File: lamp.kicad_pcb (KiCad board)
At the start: 2 copper layers, 83.8 x 40.6 mm, 18 parts, among them J1 Screw_Terminal_01x02, J2 Screw_Terminal_01x02, Q1 2N7002, U1 ESP-12E, U2 34.81-7048, U3 AMS1117-3.3

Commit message: some chnges
some changes
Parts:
- moved F1 27.5 mm to (130.2, 100.3), turned to -90 degrees
- moved U3 27.3 mm to (153.7, 124.5), turned to 180 degrees
- moved J1 24.1 mm to (121.9, 123.0)
- moved J2 20.6 mm to (121.9, 100.1)
- moved C3 12.2 mm to (167.6, 105.4), turned to -90 degrees
- moved Q1 8.54 mm to (156.2, 110.5)
- moved R6 7.86 mm to (152.4, 115.6)
- moved C4 6.87 mm to (163.8, 105.4), turned to -90 degrees
- moved C1 6.75 mm to (156.2, 118.1), turned to 0 degrees
- moved R2 6.68 mm to (176.5, 106.7)
- moved RV1 6.52 mm to (126.7, 116.8), turned to 90 degrees
- moved R3 5.56 mm to (181.6, 106.7)
- moved U2 5.43 mm to (156.5, 104.3)
- moved PS1 5.42 mm to (131.5, 121.9)
- moved R5 5.01 mm to (174.0, 129.5), turned to 90 degrees
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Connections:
- F1 pad 1: Net-(J2-Pad2) -> Net-(F1-Pad1)
- J1 pad 2: Net-(J2-Pad1) -> Net-(U2-Pad11)
- J2 pad 1: Net-(J2-Pad1) -> Net-(F1-Pad1)
- J2 pad 2: Net-(J2-Pad2) -> Net-(J1-Pad1)
- PS1 pad 2: Net-(J2-Pad1) -> Net-(J1-Pad1)
- RV1 pad 1: Net-(J2-Pad1) -> Net-(J1-Pad1)
- U2 pad 11: Net-(J1-Pad1) -> Net-(U2-Pad11)
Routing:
- net Net-(U2-Pad11): track 0.00 -> 46.1 mm
- net Net-(J2-Pad1): track 28.5 -> 0.00 mm
- net Net-(C1-Pad2): track 42.6 -> 15.1 mm
- net Net-(J1-Pad1): track 20.1 -> 33.8 mm
- net Net-(J2-Pad2): track 12.2 -> 0.00 mm
- net Net-(F1-Pad1): track 0.00 -> 8.38 mm
- net Net-(Q1-Pad1): track 44.9 -> 37.9 mm
- net Net-(C3-Pad2): track 59.3 -> 66.0 mm
- net GND: track 56.4 -> 50.0 mm
- net Net-(F1-Pad2): track 42.3 -> 39.3 mm
- net Net-(R3-Pad1): track 5.76 -> 3.13 mm
- net Net-(R2-Pad1): track 5.75 -> 3.32 mm
- net Net-(Q1-Pad3): track 7.42 -> 5.41 mm
- net Net-(R4-Pad2): track 4.44 -> 2.91 mm
- net Net-(R7-Pad1): track 4.23 -> 3.07 mm
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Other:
- board size 83.8 x 40.6 mm -> 78.7 x 36.8 mm

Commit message: Update lamp.kicad_pcb
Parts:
- moved R3 1.27 mm to (180.3, 106.7)
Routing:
- net Net-(C3-Pad2): track 66.0 -> 64.7 mm
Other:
- board size 78.7 x 36.8 mm -> 68.6 x 36.8 mm
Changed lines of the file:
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@@
   )
   (footprint "Resistor_SMD:R_0603_1608Metric" (layer "F.Cu")
-    (at 181.61 106.68 90)
+    (at 180.34 106.68 90)
     (descr "Resistor SMD 0603 (1608 Metric), square (rectangular) end terminal, IPC_7351 nominal, (Body size source: IPC-SM-782 page 72, https://www.pcb-3d.com/wordpress/wp-content/uploads/ipc-sm-782a_amendment_1_and_2.pdf), generated with kicad-footprint-generator")
     (tags "resistor")
@@
     )
   )
-  (gr_rect (start 113.03 95.25) (end 191.77 132.08) (layer "Edge.Cuts") (width 0.15) (fill none))
+  (gr_rect (start 114.3 95.25) (end 182.88 132.08) (layer "Edge.Cuts") (width 0.15) (fill none))
   (segment (start 157.4125 111.68) (end 157.16 111.4275) (width 0.25) (layer "F.Cu") (net 1))
   (segment (start 156.82 118.9375) (end 157.6475 118.11) (width 0.25) (layer "F.Cu") (net 1))
@@
   (segment (start 167.3 107.1875) (end 167.3 110.51) (width 0.25) (layer "F.Cu") (net 3))
   (segment (start 167.64 106.8475) (end 167.3 107.1875) (width 0.25) (layer "F.Cu") (net 3))
-  (segment (start 181.61 105.855) (end 176.53 105.855) (width 0.25) (layer "F.Cu") (net 3))
   (segment (start 167.64 106.8475) (end 163.83 106.8475) (width 0.25) (layer "F.Cu") (net 3))
   (segment (start 161.29 121.92) (end 161.29 115.57) (width 0.25) (layer "F.Cu") (net 3))
   (segment (start 174.79 127.6) (end 174.475 127.285) (width 0.25) (layer "F.Cu") (net 3))
   (segment (start 161.29 115.57) (end 163.83 113.03) (width 0.25) (layer "F.Cu") (net 3))
+  (segment (start 180.34 105.855) (end 176.53 105.855) (width 0.25) (layer "F.Cu") (net 3))
   (segment (start 156.82 124.46) (end 158.75 124.46) (width 0.25) (layer "F.Cu") (net 3))
   (segment (start 166.815 128.27) (end 162.0775 128.27) (width 0.25) (layer "F.Cu") (net 4))
@@
   (segment (start 152.4 116.395) (end 151.575 115.57) (width 0.25) (layer "F.Cu") (net 8))
   (segment (start 151.575 115.57) (end 155.26 111.885) (width 0.25) (layer "F.Cu") (net 8))
-  (segment (start 181.3 107.815) (end 181.3 110.51) (width 0.25) (layer "F.Cu") (net 9))
-  (segment (start 181.61 107.505) (end 181.3 107.815) (width 0.25) (layer "F.Cu") (net 9))
+  (segment (start 181.3 108.465) (end 181.3 110.51) (width 0.25) (layer "F.Cu") (net 9))
+  (segment (start 180.34 107.505) (end 181.3 108.465) (width 0.25) (layer "F.Cu") (net 9))
   (segment (start 169.3 125.71) (end 169.3 127.435) (width 0.25) (layer "F.Cu") (net 10))
   (segment (start 169.3 127.435) (end 168.465 128.27) (width 0.25) (layer "F.Cu") (net 10))

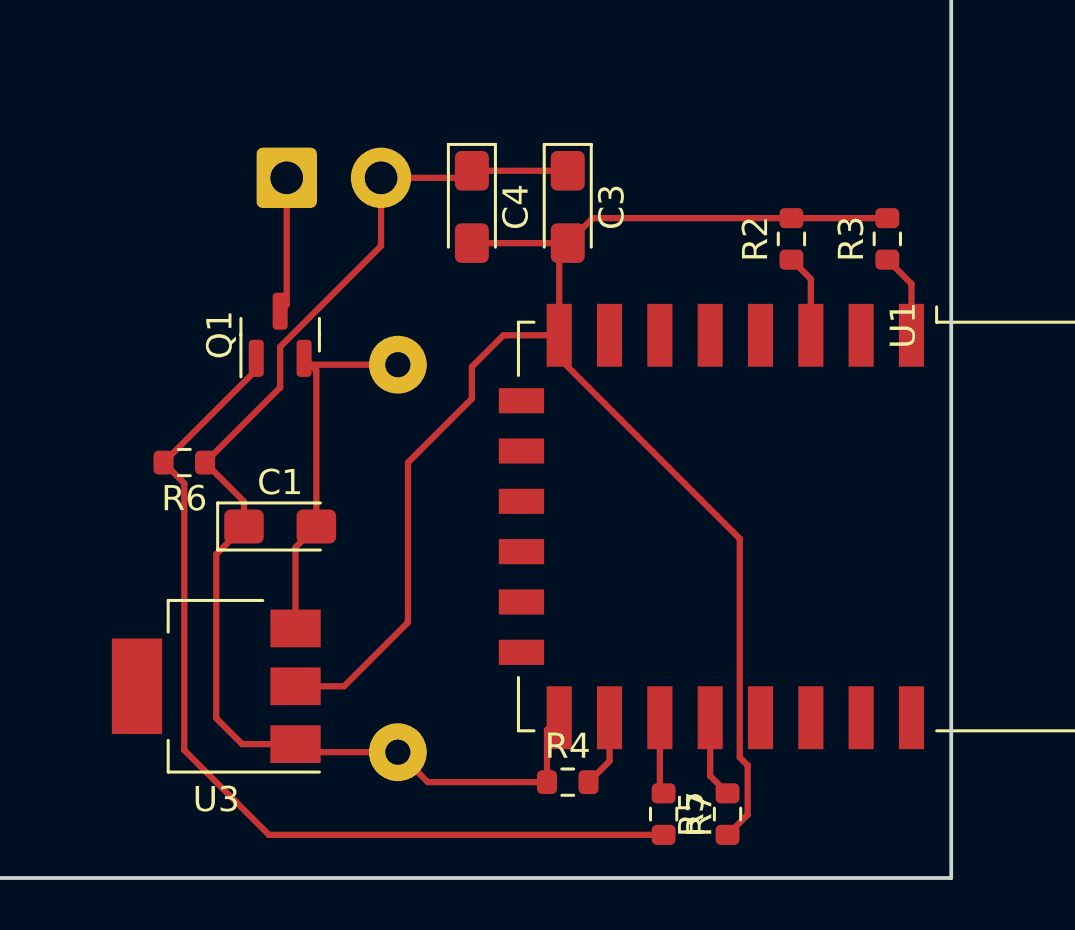
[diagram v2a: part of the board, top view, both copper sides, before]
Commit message: updated after telegram comments
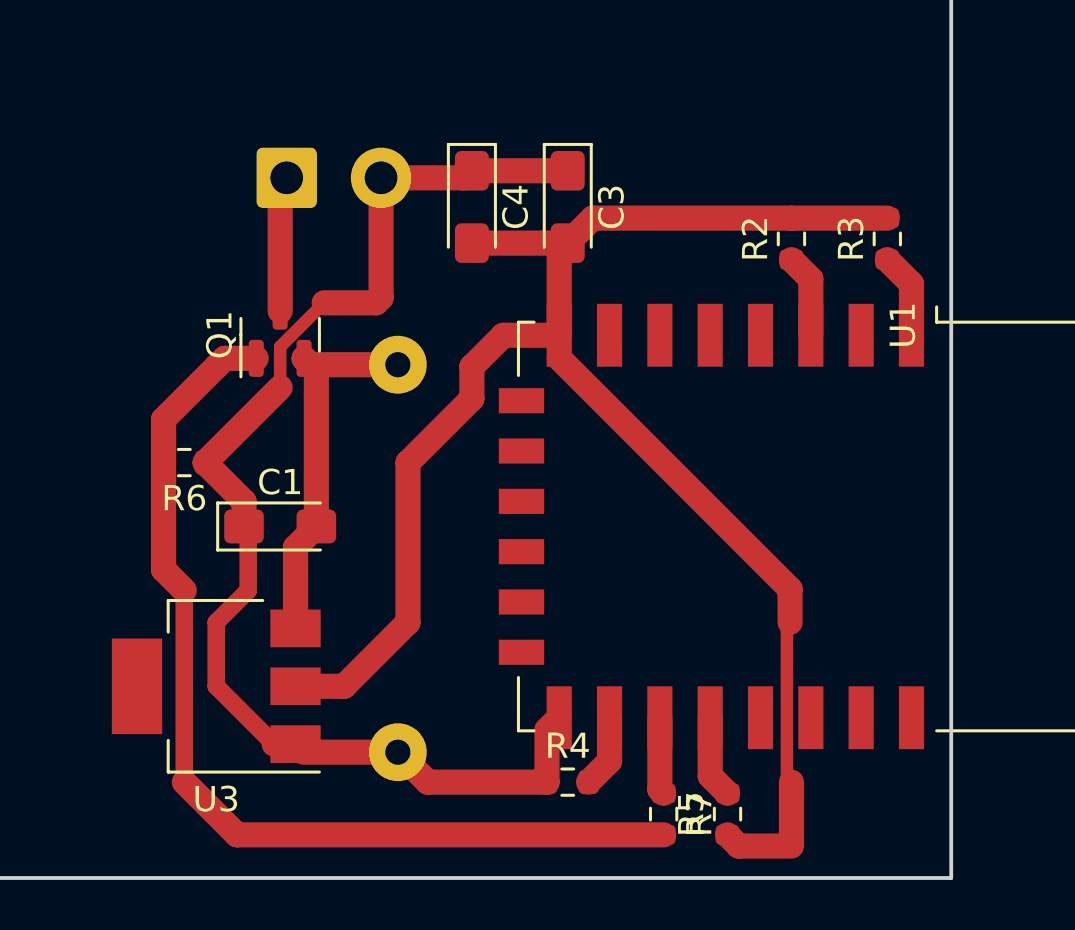
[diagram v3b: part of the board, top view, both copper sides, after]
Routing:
- net Net-(C3-Pad2): track 64.7 -> 68.4 mm
- net Net-(Q1-Pad1): track 37.9 -> 39.4 mm
- net GND: track 50.0 -> 50.6 mm

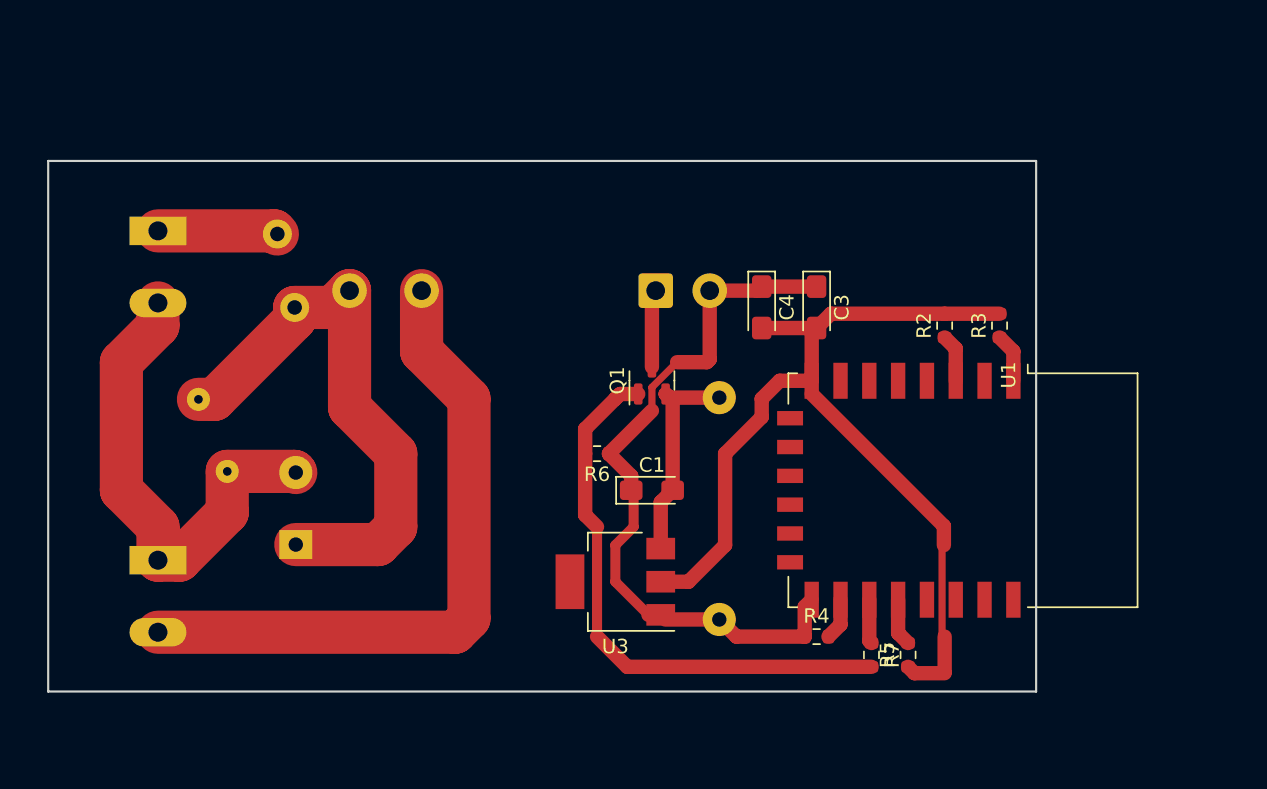
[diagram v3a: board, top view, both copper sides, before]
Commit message: 0.1 revision
broken tracing
fixed capacitor footprint
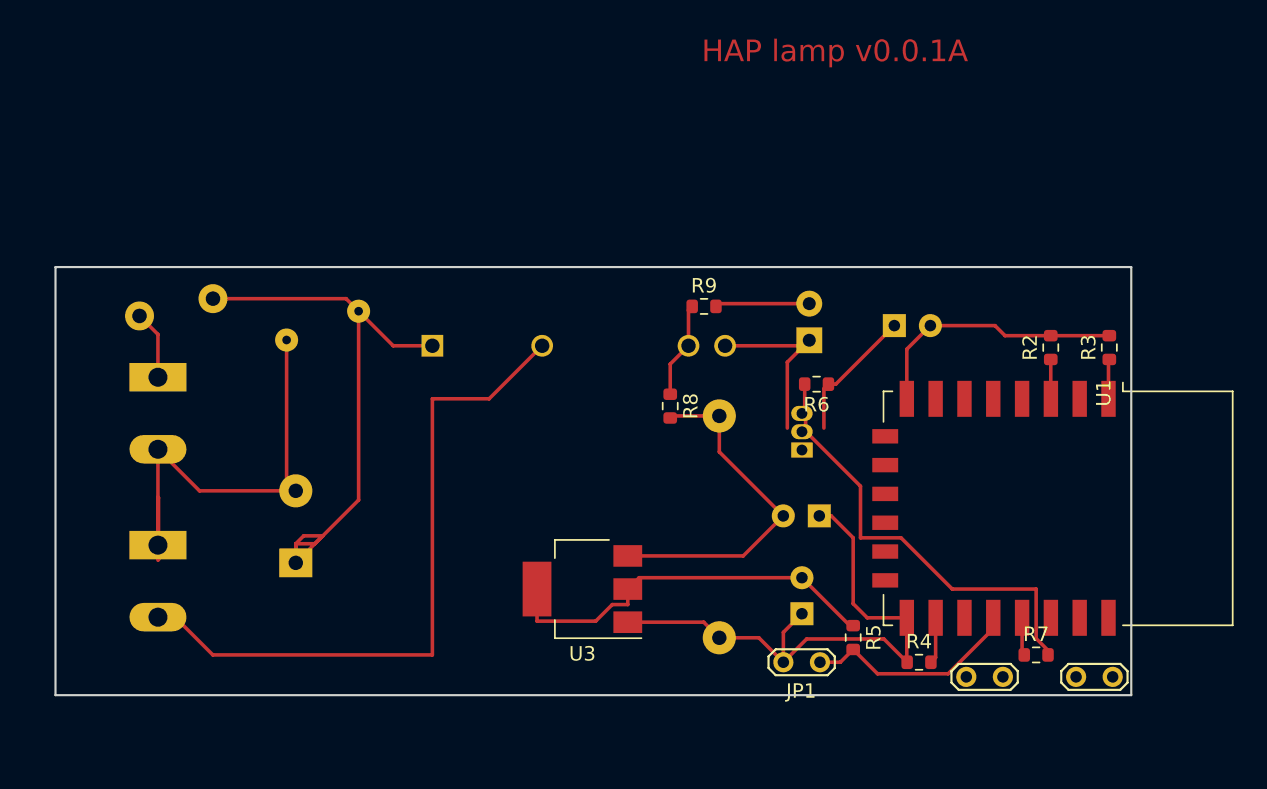
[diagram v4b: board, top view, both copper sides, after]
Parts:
- removed U2: 34.81-7048, OptoDevice:Finder_34.81
- added D1: LD274, LED_THT:LED_D5.0mm_IRGrey, B.Cu at (167.1, 107.7)
- added JP1: Jumper_2_Bridged, TestPoint:TestPoint_2Pads_Pitch2.54mm_Drill0.8mm, F.Cu at (167.9, 130.0)
- added JP2: Jumper_2_Bridged, TestPoint:TestPoint_2Pads_Pitch2.54mm_Drill0.8mm, F.Cu at (188.2, 131.1)
- added JP3: Jumper_2_Bridged, TestPoint:TestPoint_2Pads_Pitch2.54mm_Drill0.8mm, F.Cu at (180.6, 131.1)
- added K1: G3MB202PDC12, G3MB202PDC12:RELAY_G3MB202PDC12, B.Cu at (151.1, 106.7)
- added R8: 1k, Resistor_SMD:R_0603_1608Metric, F.Cu at (157.5, 112.3)
- added R9: 1k, Resistor_SMD:R_0603_1608Metric, F.Cu at (159.8, 105.3)
- C1, C3, C4: footprint Capacitor_Tantalum_SMD:CP_EIA-3216-18_Kemet-A_Pad1.58x1.35mm_HandSolder -> Capacitor_THT:CP_Radial_D5.0mm_P2.50mm; moved to B.Cu
- Q1: value 2N7002 -> BC547; footprint Package_TO_SOT_SMD:SOT-23 -> Package_TO_SOT_THT:TO-92_Inline; moved to B.Cu
- moved C4 21.5 mm to (166.6, 126.7), turned to 90 degrees
- moved R6 16.0 mm to (167.6, 110.7)
- moved C1 11.8 mm to (167.8, 119.9), turned to 180 degrees
- moved Q1 11.5 mm to (166.6, 115.3)
- moved R7 11.4 mm to (182.9, 129.5), turned to 0 degrees
- moved F1 11.1 mm to (120.6, 106.0), turned to 0 degrees
- moved J2 10.2 mm to (121.9, 110.3)
- moved RV1 10.0 mm to (130.8, 107.7), turned to 0 degrees
- moved R3 7.77 mm to (188.0, 108.2)
- moved R2 7.52 mm to (183.9, 108.2)
- moved R4 7.33 mm to (174.8, 130.0)
- moved U1 6.72 mm to (184.4, 119.4)
- moved C3 5.55 mm to (173.0, 106.7), turned to 0 degrees
- moved R5 4.00 mm to (170.2, 128.3), turned to -90 degrees
- moved U3 2.34 mm to (151.4, 125.0)
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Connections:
- C1 pad 2: Net-(C1-Pad2) -> Net-(JP2-B)
- PS1 pad 4: Net-(C1-Pad2) -> Net-(JP2-B)
- Q1 pad 1: Net-(Q1-Pad1) -> Net-(D1-K)
- Q1 pad 2: Net-(C1-Pad2) -> Net-(Q1-B)
- Q1 pad 3: Net-(Q1-Pad3) -> GND
- R6 pad 2: Net-(Q1-Pad1) -> Net-(Q1-B)
- R7 pad 1: Net-(R7-Pad1) -> Net-(U1-GPIO4)
- R7 pad 2: Net-(Q1-Pad1) -> Net-(Q1-B)
- U1 pad 17: Net-(R7-Pad1) -> unconnected-(U1-GPIO2-Pad17)
- U1 pad 19: unconnected-(U1-Pad19) -> Net-(U1-GPIO4)
- U1 pad 21: unconnected-(U1-Pad21) -> Net-(JP2-A)
- U1 pad 22: unconnected-(U1-Pad22) -> Net-(JP3-B)
- U3 pad 3: Net-(C1-Pad2) -> Net-(JP2-B)
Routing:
- net Net-(Q1-Pad1): track 39.4 -> 0.00 mm
- net Net-(Q1-B): track 0.00 -> 30.9 mm
- net Net-(JP2-B): track 0.00 -> 24.2 mm
- net Net-(U1-VCC): track 68.4 -> 45.9 mm
- net Net-(C1-Pad2): track 15.1 -> 0.00 mm
- net Net-(D1-K): track 0.00 -> 13.3 mm
- net Net-(JP1-A): track 3.29 -> 15.1 mm
- net Net-(D1-A): track 0.00 -> 7.73 mm
- net Net-(K1-+): track 0.00 -> 7.04 mm
- net Net-(Q1-Pad3): track 5.41 -> 0.00 mm
- net Net-(J2-Pin_1): track 8.38 -> 4.79 mm
- net Net-(K1-L1): track 39.3 -> 42.7 mm
- net Net-(R7-Pad1): track 3.07 -> 0.00 mm
- net Net-(U1-GPIO4): track 0.00 -> 2.70 mm
- net Net-(J1-Pin_1): track 33.8 -> 32.6 mm
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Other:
- board size 68.6 x 36.8 mm -> 74.7 x 29.7 mm
- board text added: "HAP lamp v0.0.1A"

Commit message: updated v0.0.1A
update
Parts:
- removed JP2, JP3: Jumper_2_Bridged, TestPoint:TestPoint_2Pads_Pitch2.54mm_Drill0.8mm
- added J3: Conn_01x04_Pin, Connector_PinHeader_2.54mm:PinHeader_1x04_P2.54mm_Vertical, F.Cu at (179.1, 133.3)
- added REF**: MountingHole_3.2mm_M3, MountingHole:MountingHole_3.2mm_M3, F.Cu at (119.4, 132.1)
- added REF**: MountingHole_3.2mm_M3, MountingHole:MountingHole_3.2mm_M3, F.Cu at (185.4, 104.1)
- moved R7 18.0 mm to (170.2, 116.8), turned to 90 degrees
- moved R9 3.88 mm to (160.0, 109.2)
- moved Q1 3.56 mm to (166.6, 111.8), turned to -90 degrees
- moved R8 3.30 mm to (156.2, 109.2), turned to 180 degrees
- moved U3 2.95 mm to (154.3, 125.0)
- moved F1 2.84 mm to (119.4, 103.5)
- moved R6 2.74 mm to (170.2, 111.8), turned to -90 degrees
- moved K1 2.67 mm to (151.1, 104.0)
- moved J1 2.54 mm to (121.9, 119.4)
- moved RV1 2.54 mm to (130.8, 105.1)
- moved J2 2.31 mm to (121.9, 108.0)
- moved R3 1.63 mm to (186.7, 109.2), turned to 180 degrees
- moved R2 1.44 mm to (182.9, 109.2), turned to 180 degrees
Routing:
- net Net-(J3-Pin_4): track 24.2 -> 90.7 mm
- net GND: track 50.1 -> 75.7 mm
- net Net-(Q1-B): track 30.9 -> 7.17 mm
- net Net-(U1-VCC): track 45.9 -> 59.7 mm
- net Net-(U1-GPIO4): track 2.70 -> 16.3 mm
- net Net-(J3-Pin_2): track 0.00 -> 8.16 mm
- net Net-(J3-Pin_3): track 0.00 -> 7.94 mm
- net Net-(D1-A): track 7.73 -> 13.4 mm
- net Net-(J1-Pin_2): track 47.1 -> 42.5 mm
- net Net-(K1-L1): track 42.7 -> 40.6 mm
- net Net-(J1-Pin_1): track 32.6 -> 31.0 mm
- net Net-(D1-K): track 13.3 -> 11.9 mm
- net Net-(J2-Pin_1): track 4.79 -> 5.54 mm
- net Net-(K1-+): track 7.04 -> 6.51 mm
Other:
- board size 74.7 x 29.7 mm -> 75.9 x 38.6 mm

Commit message: minor fixes
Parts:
- moved REF** 2.54 mm to (121.9, 132.1)
- moved REF** 1.80 mm to (184.2, 102.9)
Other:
- board size 75.9 x 38.6 mm -> 74.7 x 38.6 mm
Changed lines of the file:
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@@
   )
   (footprint "MountingHole:MountingHole_3.2mm_M3" (layer "F.Cu")
-    (at 119.38 132.08)
+    (at 121.92 132.08)
     (descr "Mounting Hole 3.2mm, no annular, M3")
     (tags "mounting hole 3.2mm no annular m3")
@@
   )
   (footprint "MountingHole:MountingHole_3.2mm_M3" (layer "F.Cu")
-    (at 185.42 104.14)
+    (at 184.15 102.87)
     (descr "Mounting Hole 3.2mm, no annular, M3")
     (tags "mounting hole 3.2mm no annular m3")
@@
     (property "ki_keywords" "screw terminal")
     (attr through_hole)
-    (fp_text reference "J2" (at -1.92 6.99 90) (layer "B.SilkS")
+    (fp_text reference "J2" (at -1.92 6.99 90) (layer "B.SilkS") hide
         (effects (font (size 1 1) (thickness 0.15)) (justify mirror))
     )
@@
     (property "ki_keywords" "screw terminal")
     (attr through_hole)
-    (fp_text reference "J1" (at -1.92 6.99 90) (layer "B.SilkS")
+    (fp_text reference "J1" (at -1.92 6.99 90) (layer "B.SilkS") hide
         (effects (font (size 1 1) (thickness 0.15)) (justify mirror))
     )
@@
     )
   )
-  (gr_rect (start 113.03 98.171) (end 188.976 136.779)
+  (gr_rect (start 114.3 98.171) (end 188.976 136.779)
     (stroke (width 0.15) (type solid)) (fill none) (layer "Edge.Cuts"))
   (gr_text "HAP lamp v0.0.1A" (at 137.16 133.35) (layer "F.Cu")
